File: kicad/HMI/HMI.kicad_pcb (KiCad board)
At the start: 2 copper layers, 37 x 72.8 mm, 46 parts, among them J2 SWD, J3 DEM 128128A TMH-PW-N, J4 RIBBON, SW1 SW_Push, SW10 SW_Push, SW11 SW_Push, SW12 SW_Push, SW13 SW_Push, SW14 SW_Push, SW15 SW_Push, SW16 SW_Push, SW17 SW_Push, SW18 SW_Push, SW19 SW_Push, SW2 SW_Push, SW20 SW_Push, SW3 SW_Push, SW4 SW_Push, SW5 SW_Push, SW6 SW_Push, SW7 SW_Push, SW8 SW_Push, SW9 SW_Push, U1 STM32L011K4Tx, X1 ASV-4.000MHZ-EJ-T

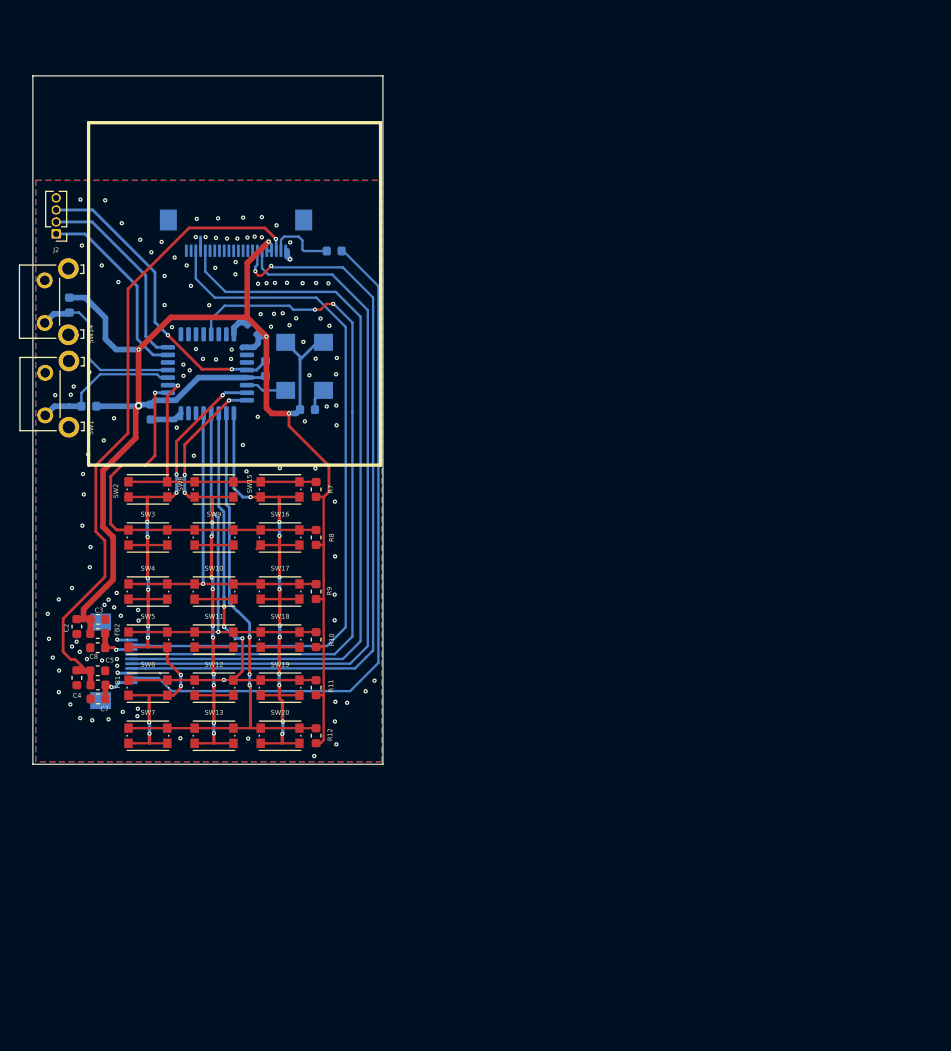
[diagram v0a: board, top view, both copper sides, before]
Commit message: HMI -> corrected PCB to mainboard form factor, added diodes
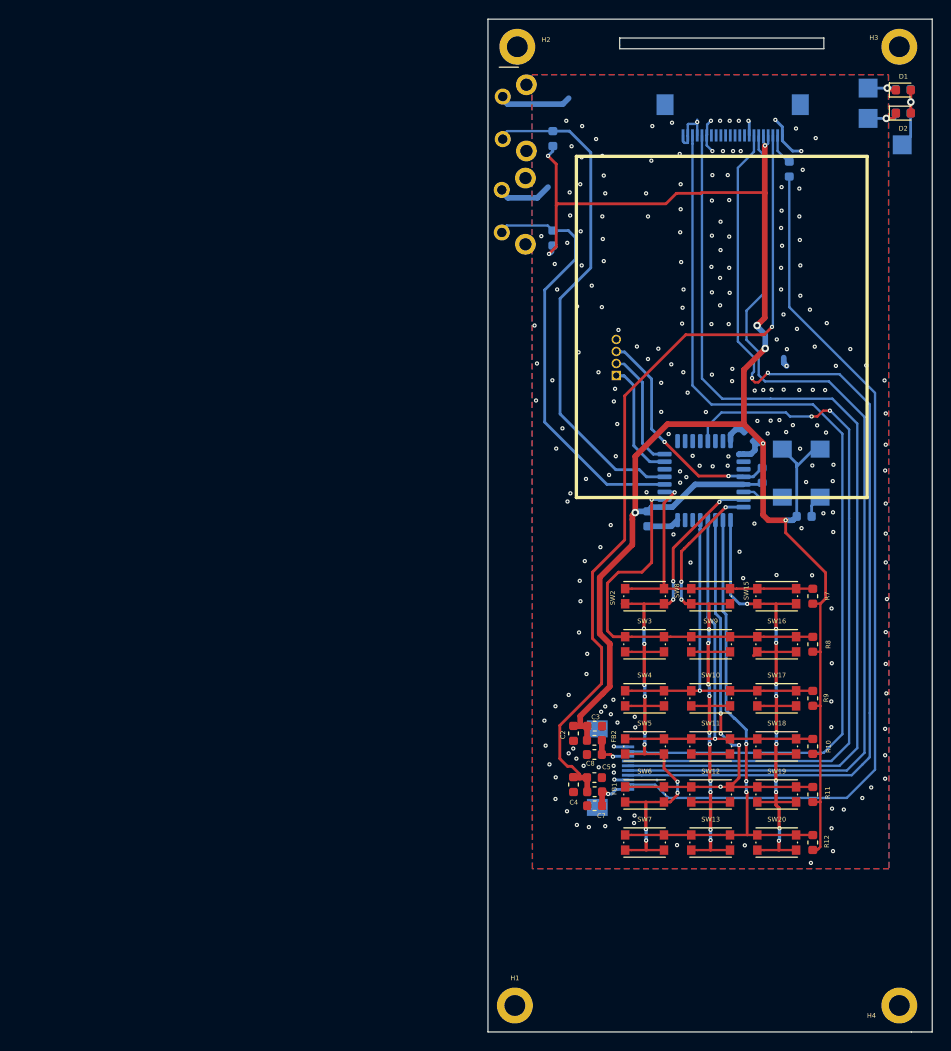
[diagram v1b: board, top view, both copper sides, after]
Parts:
- added C10: 100n, Capacitor_SMD:C_0603_1608Metric, B.Cu at (162.6, 42.2)
- added C11: 100n, Capacitor_SMD:C_0603_1608Metric, B.Cu at (162.6, 44.7)
- added D1: LED, Diode_SMD:D_0603_1608Metric, F.Cu at (162.6, 42.3)
- added D2: LED, Diode_SMD:D_0603_1608Metric, F.Cu at (162.6, 44.7)
- added H1: MountingHole_Pad, MountingHole:MountingHole_2.2mm_M2_ISO14580_Pad, F.Cu at (121.5, 139.0)
- added H2: MountingHole_Pad, MountingHole:MountingHole_2.2mm_M2_ISO14580_Pad, F.Cu at (121.8, 37.7)
- added H3: MountingHole_Pad, MountingHole:MountingHole_2.2mm_M2_ISO14580_Pad, F.Cu at (162.2, 37.7)
- added H4: MountingHole_Pad, MountingHole:MountingHole_2.2mm_M2_ISO14580_Pad, F.Cu at (162.2, 139.0)
- added TP1: TestPoint, TestPoint:TestPoint_Pad_2.0x2.0mm, B.Cu at (158.9, 42.1)
- added TP2: TestPoint, TestPoint:TestPoint_Pad_2.0x2.0mm, B.Cu at (162.5, 48.1)
- added TP3: TestPoint, TestPoint:TestPoint_Pad_2.0x2.0mm, B.Cu at (158.9, 45.3)
- J2, SW1, SW14: moved to B.Cu
- moved J2 61.1 mm to (132.2, 72.4), turned to 0 degrees
- moved R14 54.1 mm to (125.5, 47.4), turned to 90 degrees
- moved SW14 54.0 mm to (120.2, 43.0), turned to 270 degrees
- moved J3 53.9 mm to (144.5, 45.2)
- moved SW1 53.8 mm to (120.1, 52.8), turned to 270 degrees
- moved R10 53.7 mm to (153.0, 111.7)
- moved R11 53.7 mm to (153.0, 116.7)
- moved R5 53.7 mm to (147.7, 83.0)
- moved R7 53.7 mm to (153.0, 95.8)
- moved R8 53.7 mm to (153.0, 100.9)
- moved R9 53.7 mm to (153.0, 106.6)
- moved SW15 53.7 mm to (149.2, 95.8)
- moved SW16 53.7 mm to (149.2, 100.9)
- moved SW17 53.7 mm to (149.2, 106.6)
- moved SW18 53.7 mm to (149.2, 111.7)
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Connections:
- SW1 pad 1: F1 -> GND
- SW1 pad 2: GND -> F1
- SW14 pad 1: F2 -> GND
- SW14 pad 2: GND -> F2
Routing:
- net +3V3: track 159.1 -> 202.7 mm, vias 5 -> 8
- net F2: track 18.1 -> 53.7 mm
- net F1: track 15.7 -> 45.9 mm
- net GND: track 14.2 -> 42.2 mm, vias 128 -> 224
- net SPI1_SCK: track 76.1 -> 101.2 mm
- net SPI1_CS: track 80.4 -> 105.3 mm
- net TFT_RST: track 76.2 -> 99.7 mm
- net SPI1_MOSI: track 79.9 -> 103.4 mm
- net TFT_LED: track 73.2 -> 94.4 mm
- net +5V: track 68.2 -> 87.0 mm
- net Net-(C10-Pad1): track 0.00 -> 8.68 mm, vias 0 -> 1
- net SWCLK: track 21.1 -> 12.9 mm
- net NRST: track 32.6 -> 24.9 mm
- net SWDIO: track 20.4 -> 13.4 mm
- net Net-(C11-Pad2): track 0.00 -> 4.40 mm, vias 0 -> 1
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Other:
- board size 37 x 72.8 mm -> 47 x 107.1 mm

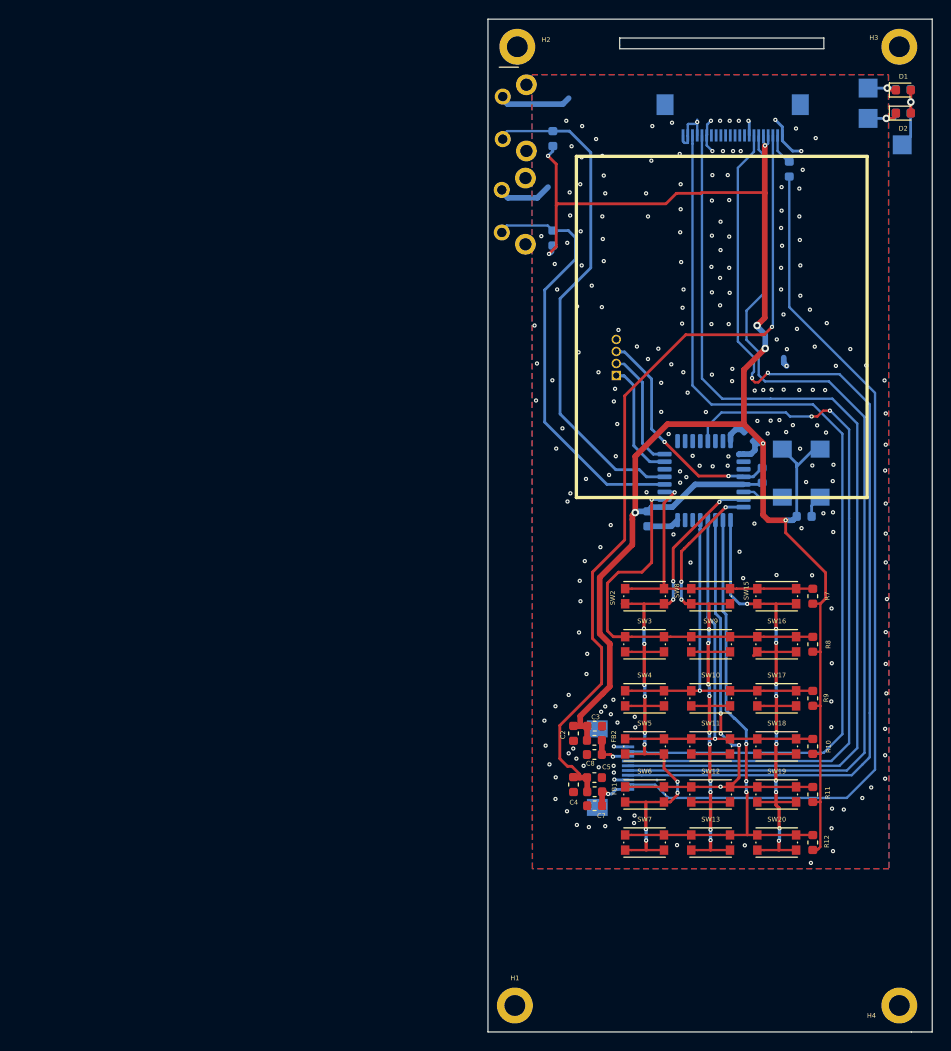
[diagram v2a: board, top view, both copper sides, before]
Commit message: HMI: widened space between keys on keypad -> generated new Gerbers & STEP
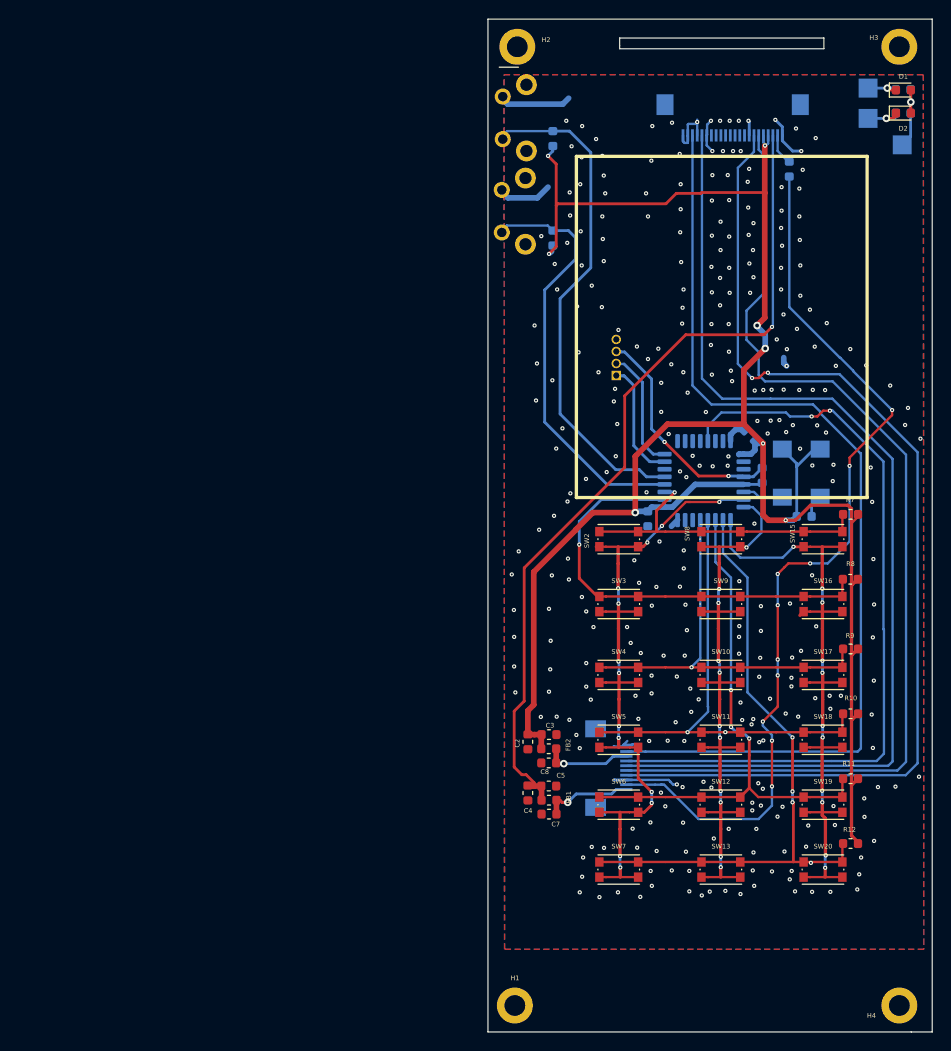
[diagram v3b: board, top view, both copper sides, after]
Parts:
- moved R7 9.53 mm to (157.0, 87.1), turned to 180 degrees
- moved R8 7.94 mm to (157.0, 94.0), turned to 180 degrees
- moved SW15 7.77 mm to (154.1, 89.7)
- moved SW2 6.62 mm to (132.5, 89.7)
- moved R9 6.58 mm to (157.0, 101.3), turned to 180 degrees
- moved SW16 6.48 mm to (154.1, 96.6)
- moved SW8 6.13 mm to (143.3, 89.7)
- moved SW20 5.66 mm to (154.1, 124.7)
- moved SW17 5.48 mm to (154.1, 104.1)
- moved R10 5.27 mm to (157.0, 108.2), turned to 180 degrees
- moved SW3 5.06 mm to (132.5, 96.6)
- moved SW19 5.01 mm to (154.1, 117.8)
- moved SW18 4.94 mm to (154.1, 111.0)
- moved C4 4.91 mm to (122.9, 116.6)
- moved FB1 4.91 mm to (125.1, 117.3)
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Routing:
- net R1: track 54.2 -> 66.9 mm, vias 3 -> 4
- net +3V3: track 202.7 -> 214.7 mm
- net C3: track 62.7 -> 72.0 mm
- net R2: track 49.9 -> 58.7 mm, vias 4 -> 3
- net R3: track 44.0 -> 51.8 mm, vias 1 -> 2
- net SPI1_SCK: track 101.2 -> 108.2 mm
- net SPI1_CS: track 105.3 -> 112.2 mm
- net SPI1_MOSI: track 103.4 -> 109.5 mm
- net C1: track 68.8 -> 74.9 mm
- net TX: track 75.7 -> 81.7 mm
- net R5: track 40.6 -> 46.4 mm
- net R4: track 37.9 -> 43.6 mm
- net GND: track 42.2 -> 47.8 mm, vias 224 -> 313
- net Net-(C7-Pad1): track 4.69 -> 9.91 mm
- net Net-(C8-Pad1): track 4.38 -> 9.50 mm
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
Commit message: HMI: some changes - not ready board YET!
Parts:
- R13, R14: moved to F.Cu
- moved J3 27.4 mm to (144.5, 72.6)
- moved R6 26.7 mm to (151.3, 77.3), turned to 180 degrees
- moved C2 7.62 mm to (122.9, 118.8)
- moved C3 7.62 mm to (125.1, 118.0)
- moved C5 7.62 mm to (125.1, 123.5)
- moved C6 7.62 mm to (135.6, 95.2)
- moved C7 7.62 mm to (125.1, 126.4)
- moved C9 7.62 mm to (146.3, 86.4)
- moved FB2 7.62 mm to (125.1, 119.5)
- moved J2 7.62 mm to (132.2, 80.1)
- moved R10 7.62 mm to (157.0, 115.8)
- moved R11 7.62 mm to (157.0, 122.7)
- moved R5 7.62 mm to (147.7, 90.6)
- moved R7 7.62 mm to (157.0, 94.7)
- moved SW10 7.62 mm to (143.3, 111.7)
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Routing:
- net SPI1_SCK: track 108.2 -> 86.8 mm
- net SPI1_CS: track 112.2 -> 91.6 mm
- net TFT_RST: track 103.2 -> 83.4 mm
- net SPI1_MOSI: track 109.5 -> 89.7 mm
- net GND: track 47.8 -> 29.9 mm, vias 313 -> 290
- net TFT_LED: track 97.0 -> 82.4 mm
- net +5V: track 89.1 -> 75.1 mm
- net +3V3: track 214.7 -> 205.8 mm, vias 8 -> 4
- net F2: track 53.7 -> 58.5 mm
- net F1: track 45.9 -> 49.4 mm
- net Net-(C7-Pad1): track 9.91 -> 11.2 mm
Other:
- outline, holes or cut-outs redrawn

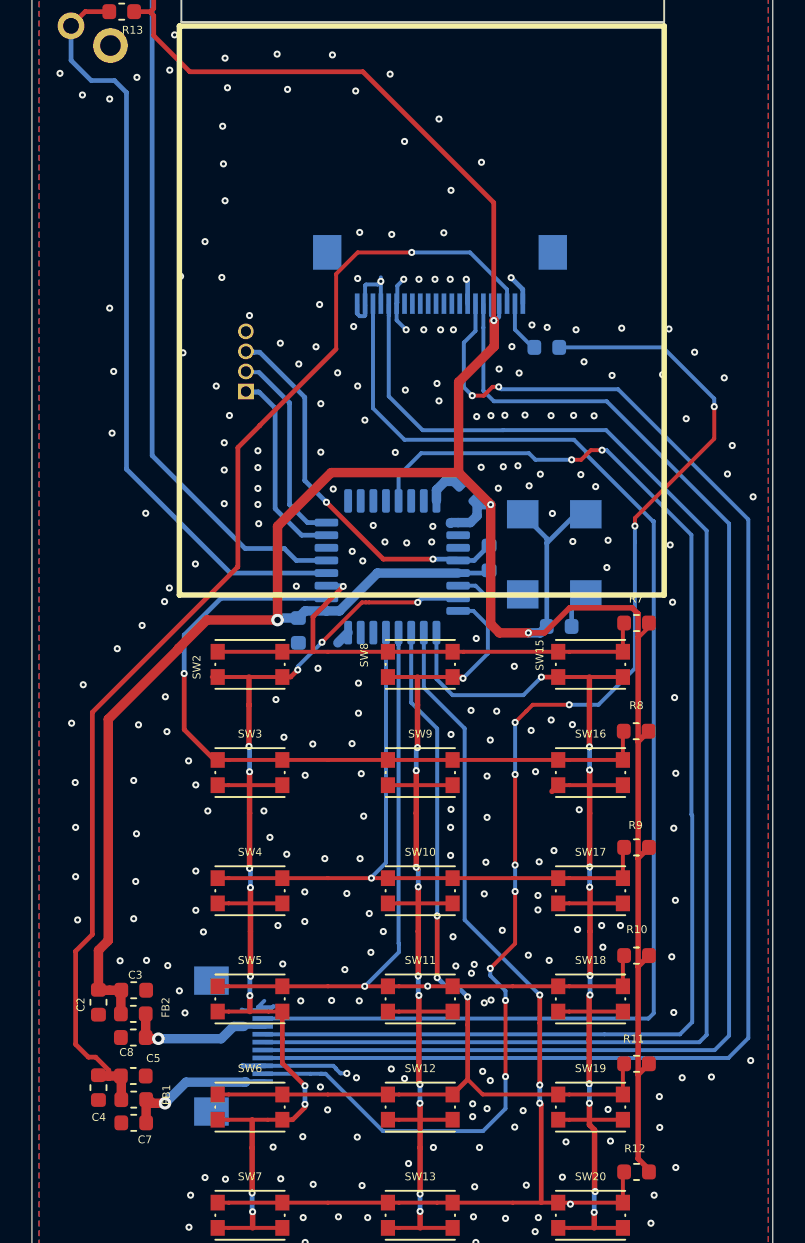
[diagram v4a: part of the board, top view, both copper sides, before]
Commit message: HMI: Added space over display + Mainboard connector placement correction -> Generated GERBER + STEP + 3D visualisation
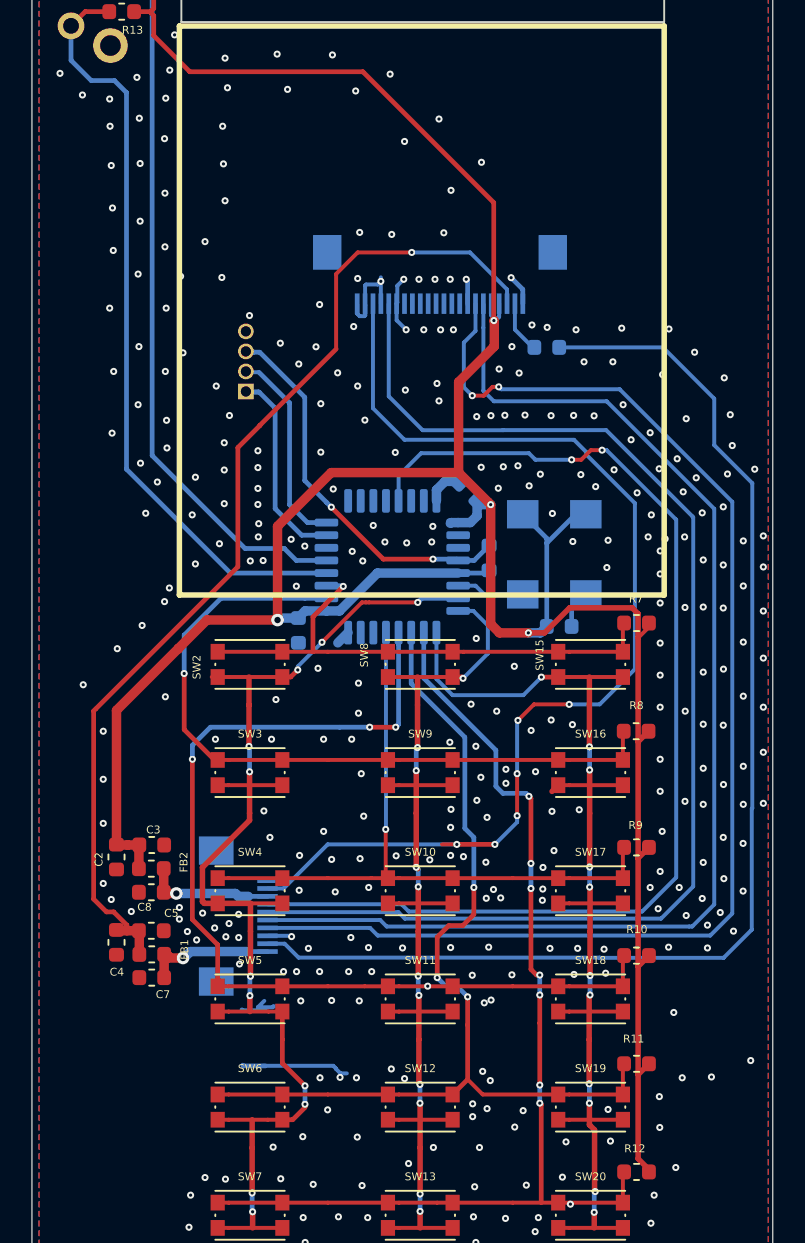
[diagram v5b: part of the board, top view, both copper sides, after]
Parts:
- moved C2 9.28 mm to (124.0, 109.6)
- moved C3 9.28 mm to (126.3, 108.8)
- moved C4 9.28 mm to (124.0, 115.0)
- moved C5 9.28 mm to (126.2, 114.2)
- moved C7 9.28 mm to (126.3, 117.2)
- moved C8 9.28 mm to (126.2, 111.8)
- moved FB1 9.28 mm to (126.3, 115.7)
- moved FB2 9.28 mm to (126.2, 110.3)
- moved J4 8.25 mm to (131.8, 113.3)
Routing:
- net R3: track 51.8 -> 63.8 mm, vias 2 -> 4
- net TFT_RST: track 83.4 -> 72.6 mm, vias 0 -> 6
- net TX: track 81.7 -> 71.8 mm
- net SPI1_MOSI: track 89.7 -> 79.8 mm
- net +5V: track 75.1 -> 65.4 mm
- net +3V3: track 205.8 -> 196.2 mm
- net SPI1_SCK: track 86.8 -> 77.4 mm
- net SPI1_CS: track 91.6 -> 82.4 mm
- net TFT_LED: track 82.4 -> 77.7 mm, vias 10 -> 0
- net R2: track 58.7 -> 61.1 mm
- net C1: track 74.9 -> 77.0 mm, vias 13 -> 11
- net GND: track 29.9 -> 31.5 mm, vias 290 -> 386
- net Net-(C8-Pad1): track 9.71 -> 8.18 mm
- net Net-(C7-Pad1): track 11.2 -> 9.78 mm
- net R1: track 66.9 -> 67.9 mm, vias 4 -> 8
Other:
- board text added: "Pcb design by Nikoloz SO3ALG Schematic by Wojtek SP5WWP"
- board text added: "SN:"
- board text added: "TR-9 HMI"
- board text added: "write something:"
